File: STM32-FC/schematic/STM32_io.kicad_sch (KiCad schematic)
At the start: 27 parts, among them IC1 STM32F746NGH6, Q1 PMDPB30XN

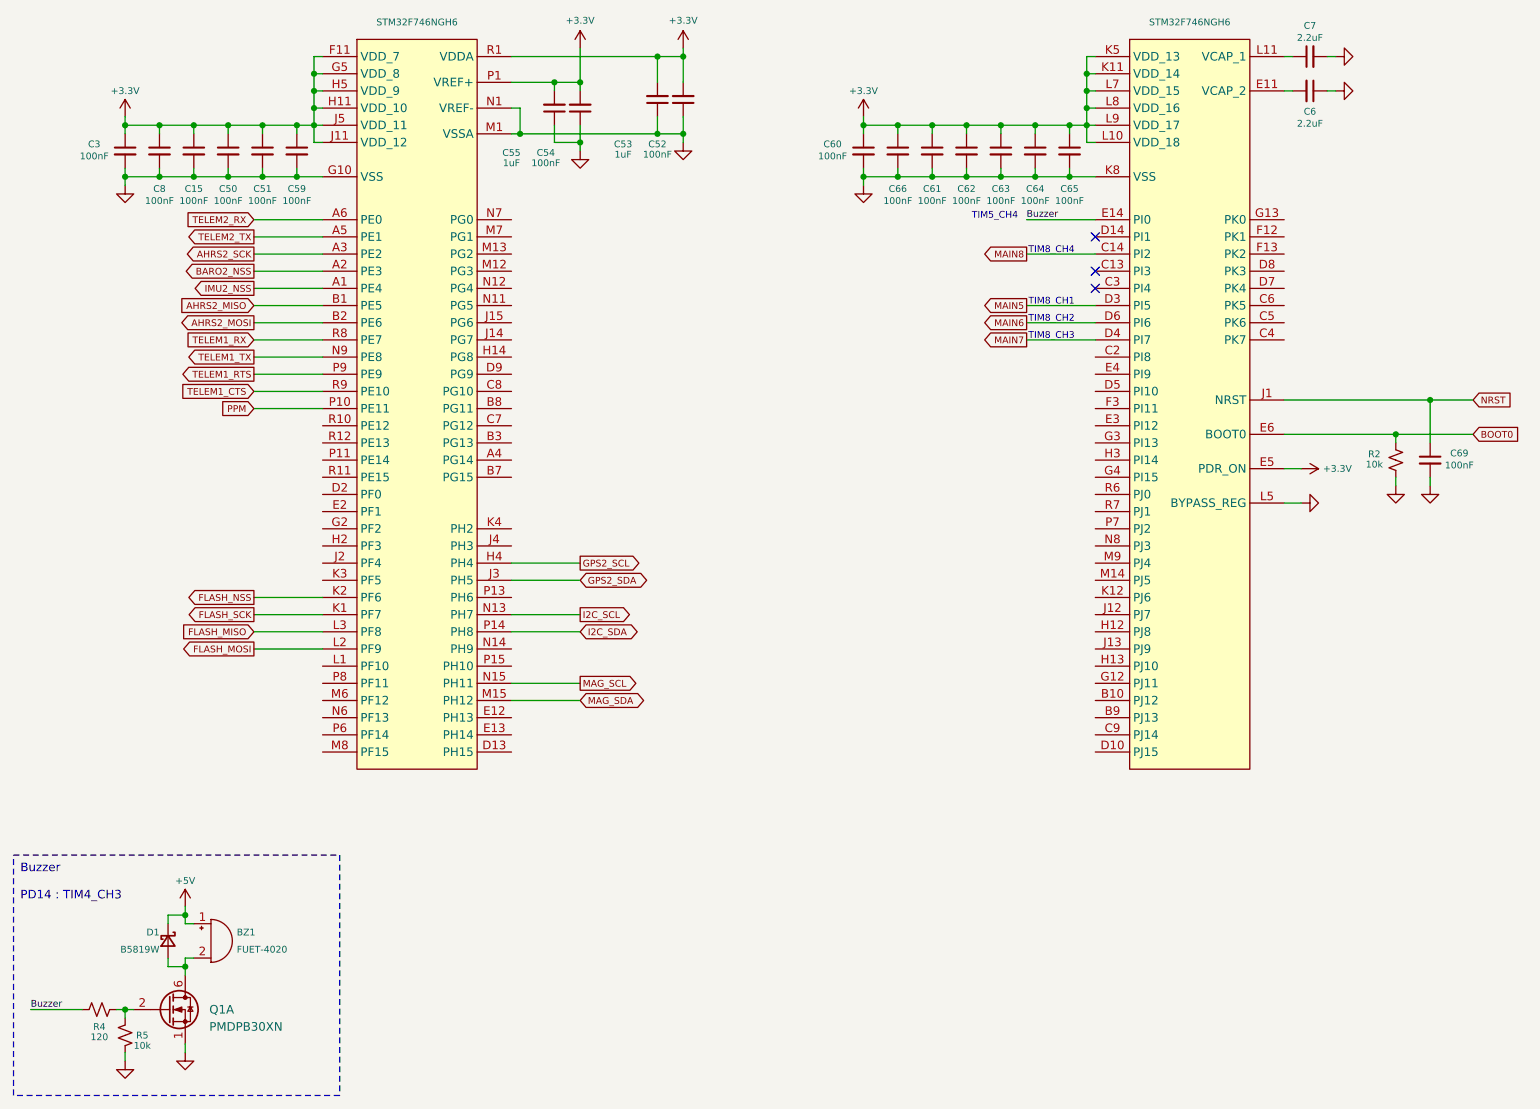
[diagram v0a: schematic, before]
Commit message: add DJI Air unit and RC Selector
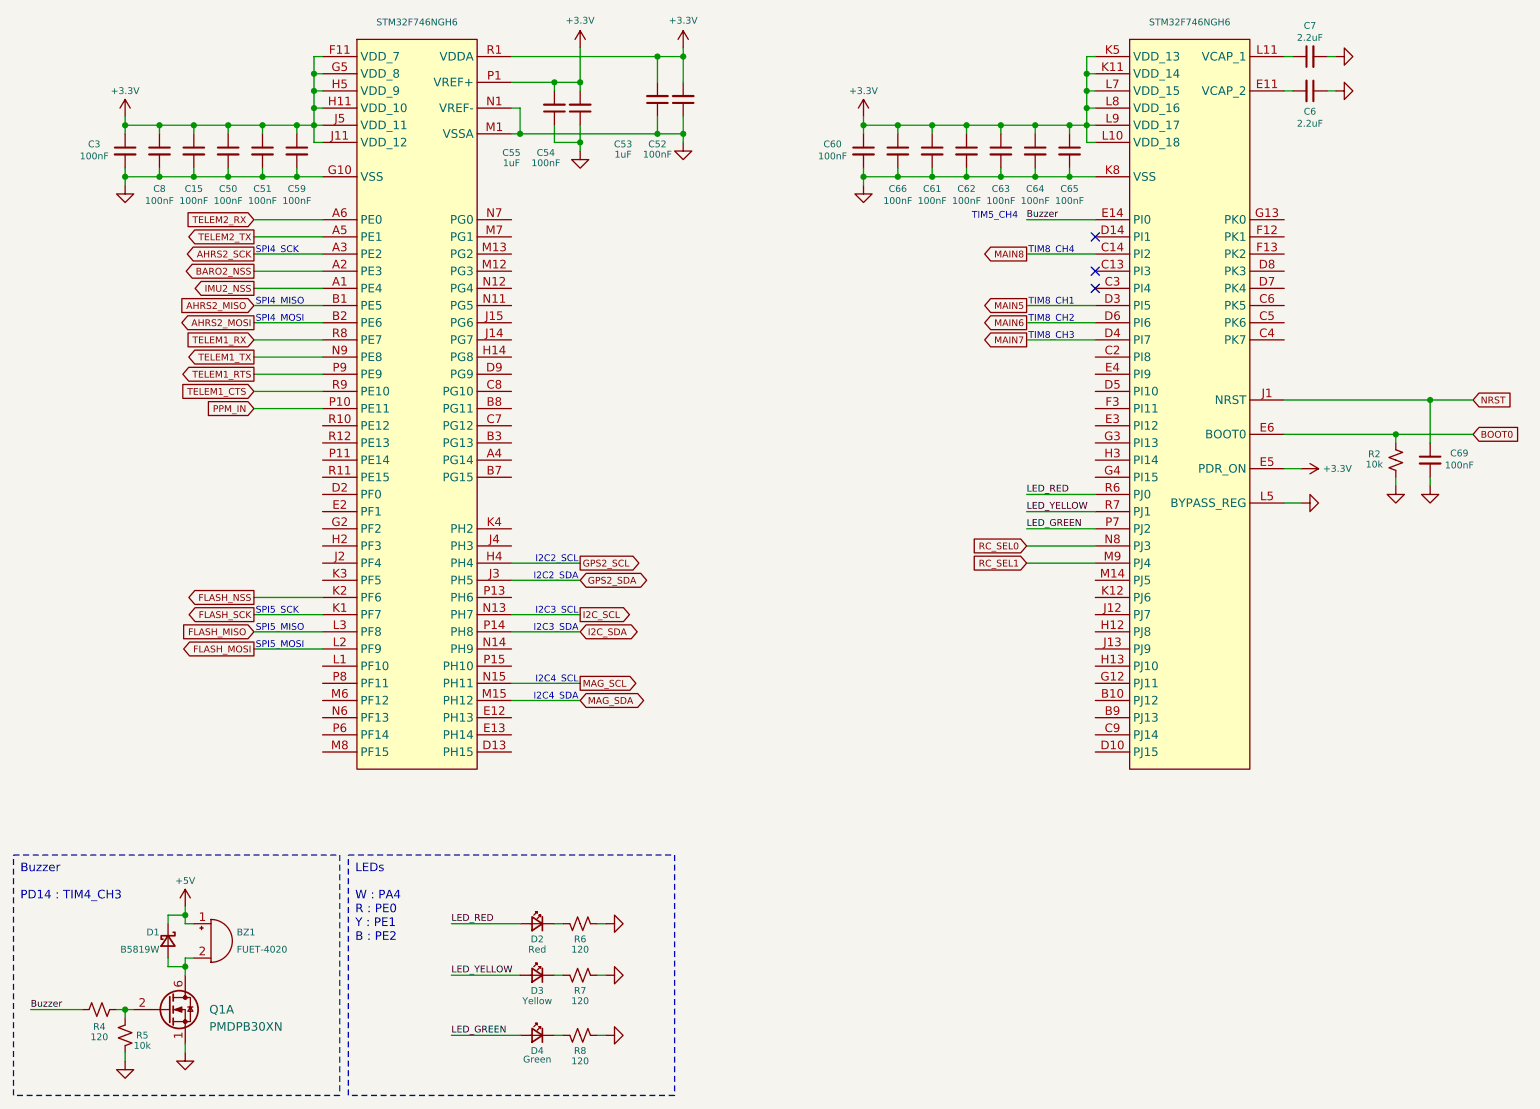
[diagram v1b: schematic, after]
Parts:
- added D2: Red, LED_SMD:LED_0402_1005Metric, symbol Device:LED_Small
- added D3: Yellow, LED_SMD:LED_0402_1005Metric, symbol Device:LED_Small
- added D4: Green, LED_SMD:LED_0402_1005Metric, symbol Device:LED_Small
- added R6, R7, R8: 120, Resistor_SMD:R_0402_1005Metric, symbol Device:R_Small_US
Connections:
- net GND: now also R6.2, R7.2, R8.2
- net RC_SEL1: now reaches IC1.M9 (PJ4)
- net RC_SEL0: now reaches IC1.N8 (PJ3)
- net LED_GREEN: now reaches IC1.P7 (PJ2)
- net LED_GREEN: now also D4.2 (A)
- net LED_RED: now reaches IC1.R6 (PJ0)
- net LED_RED: now also D2.2 (A)
- net LED_YELLOW: now reaches IC1.R7 (PJ1)
- net LED_YELLOW: now also D3.2 (A)
- net PPM renamed PPM_IN
- new net: D3.1 (K), R7.1
- new net: D4.1 (K), R8.1
- new net: D2.1 (K), R6.1
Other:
- note added: "I2C2_SCL"
- note added: "I2C2_SDA"
- note added: "I2C3_SCL"
- note added: "I2C3_SDA"
- note added: "I2C4_SCL"
- note added: "I2C4_SDA"
- note added: "LEDs"
- note added: "SPI4_MISO"
- note added: "SPI4_MOSI"
- note added: "SPI4_SCK"
- note added: "SPI5_MISO"
- note added: "SPI5_MOSI"
- note added: "SPI5_SCK"
- note added: "W : PA4 R : PE0 Y : PE1 B : PE2"

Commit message: ERC passed
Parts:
- renumbered C3 to C10, C8 to C11, C15 to C12, C50 to C13, C51 to C14, C59 to C15, C55 to C16, C54 to C17, C53 to C18, C52 to C19, C60 to C20, C66 to C21, C61 to C22, C62 to C23, C63 to C24, C64 to C25, C65 to C26, C7 to C27, C6 to C28, C69 to C29, R4 to R2, R5 to R3, R6 to R4, R7 to R5, R8 to R6, R2 to R7
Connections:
- net SW_PWR_A: now reaches IC1.K12 (PJ6)
- net SW_PWR_IMU: now reaches IC1.M14 (PJ5)
- no-connect marks 3 -> 68
